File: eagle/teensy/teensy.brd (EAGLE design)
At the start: 51.7 x 35.5 mm, 4 parts

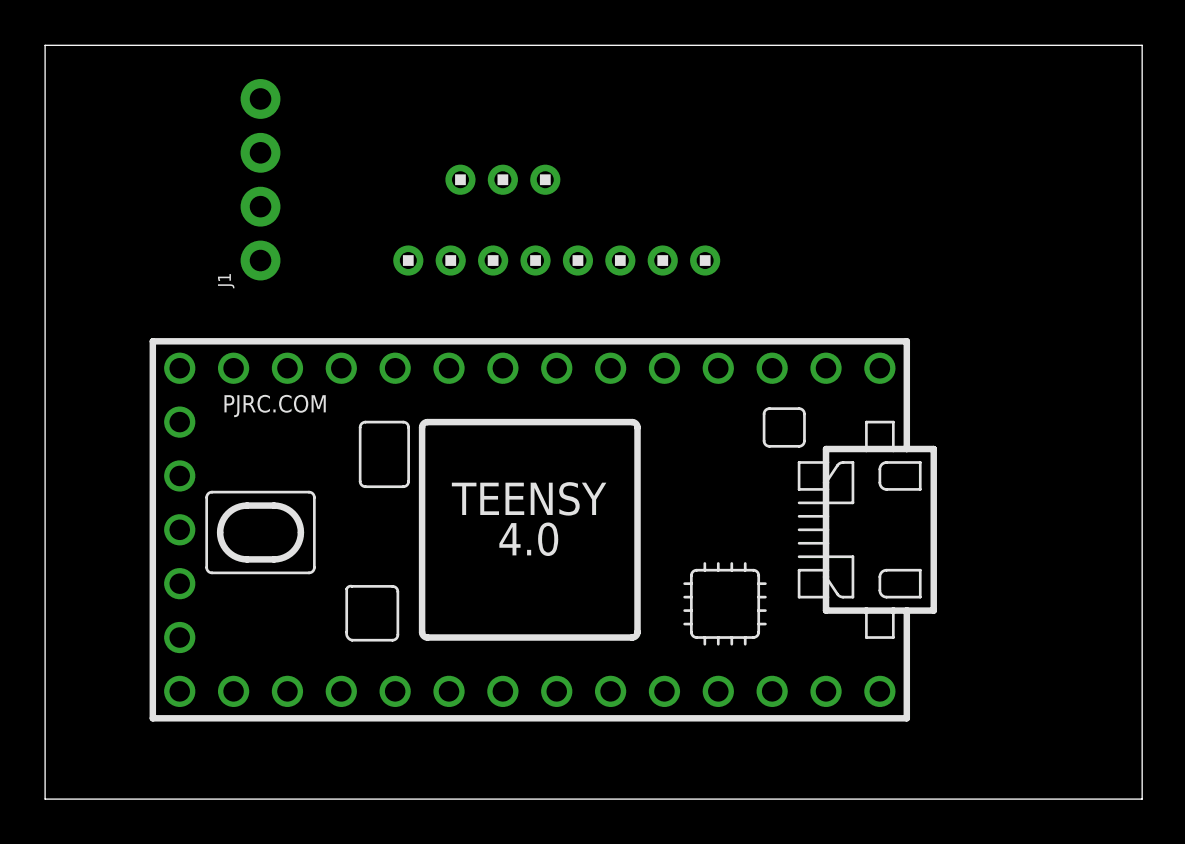
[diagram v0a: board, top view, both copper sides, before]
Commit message: modified:   eagle/teensy/teensy.brd
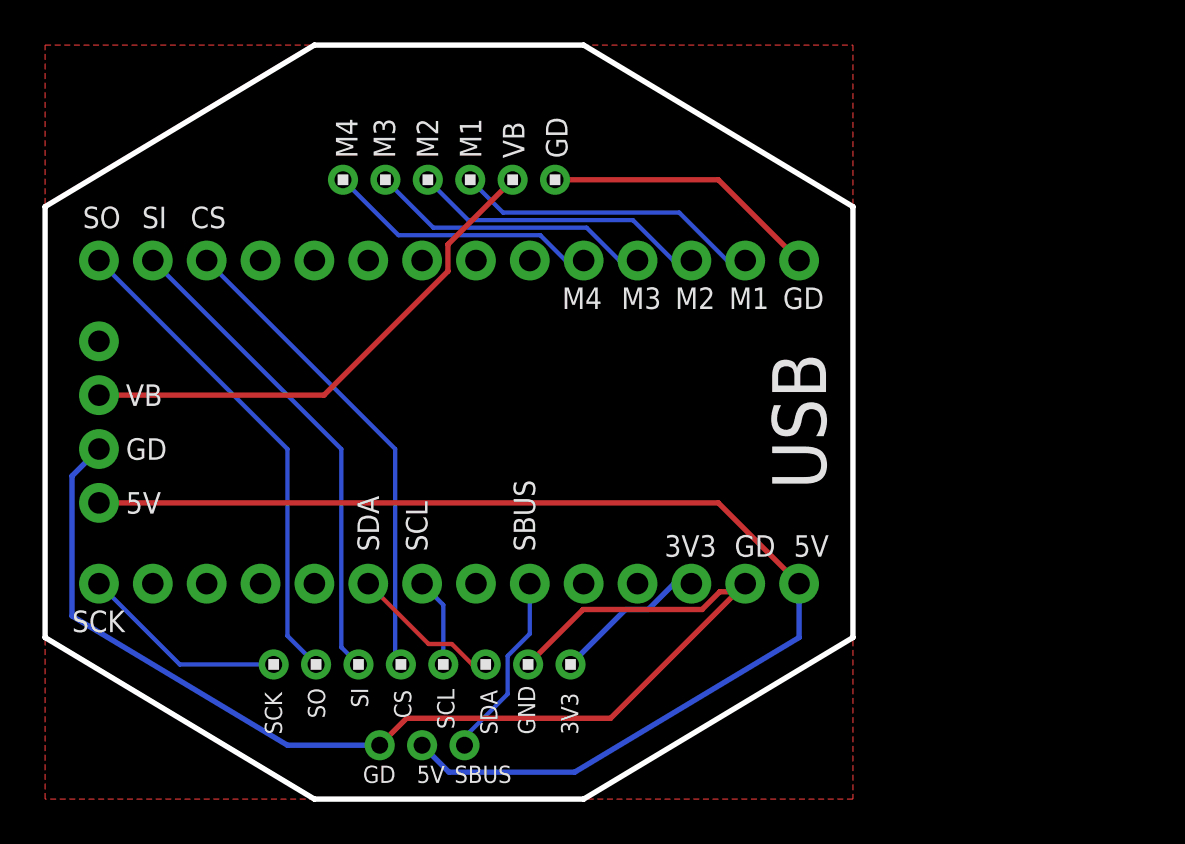
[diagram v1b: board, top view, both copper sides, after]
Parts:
- removed U$1: TEENSY_4.0, TEENSY 4.0:TEENSY_4.0
- added J2, J3: (no value), SparkFun-Connectors:1X14_NO_SILK
- added U$4: 1X6, headers(2mm):1X6
- moved U$2 26.9 mm to (17.8, 2.54), flipped to the bottom, turned to 180 degrees
- moved U$3 20.1 mm to (17.8, 6.35), turned to 180 degrees
- moved J1 8.52 mm to (2.54, 21.6), turned to 270 degrees
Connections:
- new net M1: J2.13, U$4.3
- new net M2: J2.12, U$4.4
- new net M3: J2.11, U$4.5
- new net M4: J2.10, U$4.6
- net 3V3: now also J3.12
- net 5V: now also J3.14
- net CS: now also J2.3, U$3.5; no longer U$3.8
- net GND: now also J2.14, J3.13, U$4.1
- net MISO: now also J2.1, U$3.7; no longer U$3.5
- net MOSI: now also J2.2
- net SBUS: now also J3.9
- net SCK: now also J3.1, U$3.8; no longer U$3.7
- net SCL: now also J3.7, U$3.4; no longer U$3.3
- net SDA: now also J3.6, U$3.3; no longer U$3.4
- net VBAT: now also U$4.2
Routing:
- net GND: track 0.00 -> 69.4 mm
- net 5V: track 0.00 -> 57.2 mm
- net VBAT: track 0.00 -> 24.5 mm
- net MISO: track 0.00 -> 23.3 mm
- net MOSI: track 0.00 -> 23.1 mm
- net CS: track 0.00 -> 22.8 mm
- net M1: track 0.00 -> 14.5 mm
- net M2: track 0.00 -> 14.0 mm
- net M3: track 0.00 -> 13.5 mm
- net M4: track 0.00 -> 12.9 mm
- net SCK: track 0.00 -> 9.82 mm
- net SBUS: track 0.00 -> 8.51 mm
- net 3V3: track 0.00 -> 7.28 mm
- net SDA: track 0.00 -> 7.12 mm
- net SCL: track 0.00 -> 4.22 mm
- added copper zone on layer 1, net GND
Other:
- board size 51.7 x 35.5 mm -> 38.1 x 35.6 mm
- board text added: "3V3"
- board text added: "5V"
- board text added: "CS"
- board text added: "GD"
- board text added: "GND"
- board text added: "M1"
- board text added: "M2"
- board text added: "M3"
- board text added: "M4"
- board text added: "SBUS"
- board text added: "SCK"
- board text added: "SCL"
- board text added: "SDA"
- board text added: "SI"
- board text added: "SO"
- board text added: "USB"
- board text added: "VB"

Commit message: modified:   eagle/teensy/teensy.brd
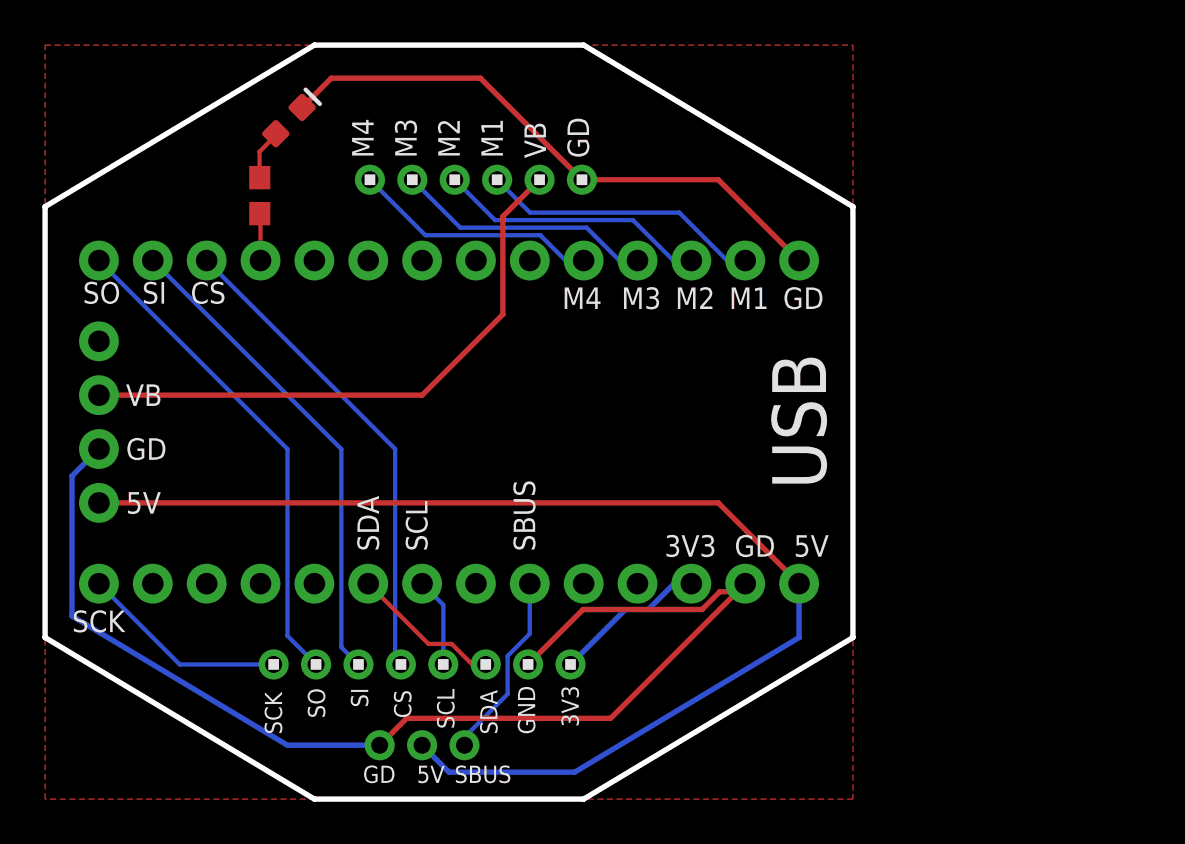
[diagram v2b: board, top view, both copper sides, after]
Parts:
- added D1: WHITE, SparkFun-LED:LED-0603
- added R1: 22, SparkFun-Resistors:0603
- moved U$4 1.27 mm to (20.3, 29.2)
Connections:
- new net R1: J2.4, R1.1
- new net R2: D1.A, R1.2
- net GND: now also D1.C
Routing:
- net GND: track 69.4 -> 83.8 mm
- net VBAT: track 24.5 -> 27.7 mm
- net R2: track 0.00 -> 2.39 mm
- net R1: track 0.00 -> 2.22 mm
- net M2: track 14.0 -> 12.7 mm
- net M4: track 12.9 -> 11.7 mm
- net M3: track 13.5 -> 12.2 mm
- net M1: track 14.5 -> 13.3 mm
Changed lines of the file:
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@@
 <setting verticaltext="up"/>
 </settings>
-<grid distance="10" unitdist="mil" unit="mil" style="lines" multiple="1" display="no" altdistance="5" altunitdist="mil" altunit="mil"/>
+<grid distance="0.000123031496" unitdist="mil" unit="mil" style="lines" multiple="1" display="no" altdistance="5" altunitdist="mil" altunit="mil"/>
 <layers>
 <layer number="1" name="Top" color="4" fill="1" visible="yes" active="yes"/>
@@
 <wire x1="12.7" y1="35.56" x2="25.4" y2="35.56" width="0.254" layer="20"/>
 <text x="36.83" y="14.605" size="2.54" layer="21" rot="R90">USB</text>
-<text x="14.732" y="30.226" size="1.016" layer="25" rot="R90">M4</text>
-<text x="16.51" y="30.226" size="1.016" layer="25" rot="R90">M3</text>
-<text x="18.542" y="30.226" size="1.016" layer="25" rot="R90">M2</text>
-<text x="20.574" y="30.226" size="1.016" layer="25" rot="R90">M1</text>
+<text x="15.494" y="30.226" size="1.016" layer="25" rot="R90">M4</text>
+<text x="17.526" y="30.226" size="1.016" layer="25" rot="R90">M3</text>
+<text x="19.558" y="30.226" size="1.016" layer="25" rot="R90">M2</text>
+<text x="21.59" y="30.226" size="1.016" layer="25" rot="R90">M1</text>
 <text x="3.81" y="18.542" size="1.016" layer="25">VB</text>
 <text x="3.81" y="16.002" size="1.016" layer="25">GD</text>
@@
 <text x="32.258" y="23.114" size="1.016" layer="25">M1</text>
 <text x="34.798" y="23.114" size="1.016" layer="25">GD</text>
-<text x="1.778" y="26.924" size="1.016" layer="25">SO</text>
-<text x="4.572" y="26.924" size="1.016" layer="25">SI</text>
-<text x="6.858" y="26.924" size="1.016" layer="25">CS</text>
-<text x="22.606" y="30.226" size="1.016" layer="25" rot="R90">VB</text>
-<text x="24.638" y="30.226" size="1.016" layer="25" rot="R90">GD</text>
+<text x="1.778" y="23.368" size="1.016" layer="25">SO</text>
+<text x="4.572" y="23.368" size="1.016" layer="25">SI</text>
+<text x="6.858" y="23.368" size="1.016" layer="25">CS</text>
+<text x="23.622" y="30.226" size="1.016" layer="25" rot="R90">VB</text>
+<text x="25.654" y="30.226" size="1.016" layer="25" rot="R90">GD</text>
 <text x="3.81" y="13.462" size="1.016" layer="25">5V</text>
 <text x="35.306" y="11.43" size="1.016" layer="25">5V</text>
@@
 <text x="21.336" y="3.048" size="0.8128" layer="25" rot="R90">SDA</text>
 <text x="23.114" y="3.048" size="0.8128" layer="25" rot="R90">GND</text>
-<text x="25.146" y="3.048" size="0.8128" layer="25" rot="R90">3V3</text>
+<text x="25.1709125" y="3.397071875" size="0.8128" layer="25" rot="R90">3V3</text>
 <text x="14.986" y="0.762" size="0.8128" layer="25">GD</text>
 <text x="17.526" y="0.762" size="0.8128" layer="25">5V</text>
@@
 <element name="U$2" library="headers(2mm)" package="1X3" value="1X3" x="17.78" y="2.54" smashed="yes" rot="MR180"/>
 <element name="U$3" library="headers(2mm)" package="1X8" value="1X8" x="17.78" y="6.35" smashed="yes" rot="R180"/>
-<element name="U$4" library="headers(2mm)" package="1X6" value="1X6" x="19.05" y="29.21" rot="R180"/>
+<element name="U$4" library="headers(2mm)" package="1X6" value="1X6" x="20.32" y="29.21" rot="R180"/>
 <element name="J2" library="SparkFun-Connectors" package="1X14_NO_SILK" value="" x="2.54" y="25.4" smashed="yes">
 <attribute name="VALUE" x="1.27" y="23.368" size="0.6096" layer="27" font="vector" ratio="20"/>
@@
 <element name="J3" library="SparkFun-Connectors" package="1X14_NO_SILK" value="" x="2.54" y="10.16" smashed="yes">
 <attribute name="VALUE" x="1.27" y="8.128" size="0.6096" layer="27" font="vector" ratio="20"/>
+</element>
+<element name="D1" library="SparkFun-LED" package="LED-0603" value="WHITE" x="11.5" y="32" smashed="yes" rot="R45">
+<attribute name="PROD_ID" value="DIO-09004" x="11.5" y="32" size="1.778" layer="27" rot="R45" display="off"/>
+</element>
+<element name="R1" library="SparkFun-Resistors" package="0603" value="22" x="10.12456875" y="28.458459375" smashed="yes" rot="R90">
+<attribute name="PROD_ID" value="RES-08698" x="10.12456875" y="28.458459375" size="1.778" layer="27" rot="R90" display="off"/>
 </element>
 </elements>
@@
 </polygon>
 <contactref element="J1" pad="3"/>
-<wire x1="24.05" y1="29.21" x2="31.75" y2="29.21" width="0.254" layer="1"/>
+<wire x1="25.32" y1="29.21" x2="31.75" y2="29.21" width="0.254" layer="1"/>
 <wire x1="31.75" y1="29.21" x2="35.56" y2="25.4" width="0.254" layer="1"/>
 <wire x1="26.67" y1="3.81" x2="17.05" y2="3.81" width="0.254" layer="1"/>
@@
 <wire x1="11.43" y1="2.54" x2="15.78" y2="2.54" width="0.254" layer="16"/>
 <wire x1="17.05" y1="3.81" x2="15.78" y2="2.54" width="0.254" layer="1"/>
+<contactref element="D1" pad="C"/>
+<wire x1="25.32" y1="29.21" x2="20.53" y2="34" width="0.254" layer="1"/>
+<wire x1="20.53" y1="34" x2="13.5" y2="34" width="0.254" layer="1"/>
+<wire x1="13.5" y1="34" x2="12.12013125" y2="32.62013125" width="0.254" layer="1"/>
 </signal>
 <signal name="5V">
@@
 <contactref element="J1" pad="2"/>
 <contactref element="U$4" pad="2"/>
-<wire x1="22.05" y1="29.21" x2="18.9992" y2="26.1592" width="0.254" layer="1"/>
-<wire x1="18.9992" y1="26.1592" x2="18.9992" y2="24.8949875" width="0.254" layer="1"/>
-<wire x1="18.9992" y1="24.8949875" x2="13.1542125" y2="19.05" width="0.254" layer="1"/>
-<wire x1="13.1542125" y1="19.05" x2="2.54" y2="19.05" width="0.254" layer="1"/>
+<wire x1="23.32" y1="29.21" x2="21.59" y2="27.48" width="0.254" layer="1"/>
+<wire x1="21.59" y1="27.48" x2="21.59" y2="22.86" width="0.254" layer="1"/>
+<wire x1="21.59" y1="22.86" x2="17.78" y2="19.05" width="0.254" layer="1"/>
+<wire x1="17.78" y1="19.05" x2="2.54" y2="19.05" width="0.254" layer="1"/>
 </signal>
 <signal name="SBUS">
@@
 <contactref element="U$4" pad="3"/>
 <contactref element="J2" pad="13"/>
-<wire x1="20.05" y1="29.21" x2="21.5994" y2="27.6606" width="0.2032" layer="16"/>
+<wire x1="21.32" y1="29.21" x2="22.8694" y2="27.6606" width="0.2032" layer="16"/>
 <wire x1="32.16829375" y1="25.4" x2="33.02" y2="25.4" width="0.2032" layer="16"/>
-<wire x1="21.5994" y1="27.6606" x2="29.90769375" y2="27.6606" width="0.2032" layer="16"/>
+<wire x1="22.8694" y1="27.6606" x2="29.90769375" y2="27.6606" width="0.2032" layer="16"/>
 <wire x1="29.90769375" y1="27.6606" x2="32.16829375" y2="25.4" width="0.2032" layer="16"/>
 </signal>
@@
 <contactref element="U$4" pad="4"/>
 <contactref element="J2" pad="12"/>
-<wire x1="18.05" y1="29.21" x2="19.955" y2="27.305" width="0.2032" layer="16"/>
+<wire x1="19.32" y1="29.21" x2="21.225" y2="27.305" width="0.2032" layer="16"/>
 <wire x1="29.62829375" y1="25.4" x2="30.48" y2="25.4" width="0.2032" layer="16"/>
-<wire x1="19.955" y1="27.305" x2="27.72329375" y2="27.305" width="0.2032" layer="16"/>
+<wire x1="21.225" y1="27.305" x2="27.72329375" y2="27.305" width="0.2032" layer="16"/>
 <wire x1="27.72329375" y1="27.305" x2="29.62829375" y2="25.4" width="0.2032" layer="16"/>
 </signal>
@@
 <contactref element="U$4" pad="5"/>
 <contactref element="J2" pad="11"/>
-<wire x1="16.05" y1="29.21" x2="18.3106" y2="26.9494" width="0.2032" layer="16"/>
+<wire x1="17.32" y1="29.21" x2="19.5806" y2="26.9494" width="0.2032" layer="16"/>
 <wire x1="27.08829375" y1="25.4" x2="27.94" y2="25.4" width="0.2032" layer="16"/>
-<wire x1="18.3106" y1="26.9494" x2="25.53889375" y2="26.9494" width="0.2032" layer="16"/>
+<wire x1="19.5806" y1="26.9494" x2="25.53889375" y2="26.9494" width="0.2032" layer="16"/>
 <wire x1="25.53889375" y1="26.9494" x2="27.08829375" y2="25.4" width="0.2032" layer="16"/>
 </signal>
@@
 <contactref element="U$4" pad="6"/>
 <contactref element="J2" pad="10"/>
-<wire x1="14.05" y1="29.21" x2="16.6662" y2="26.5938" width="0.2032" layer="16"/>
+<wire x1="15.32" y1="29.21" x2="17.9362" y2="26.5938" width="0.2032" layer="16"/>
 <wire x1="24.54829375" y1="25.4" x2="25.4" y2="25.4" width="0.2032" layer="16"/>
 <wire x1="23.35449375" y1="26.5938" x2="24.54829375" y2="25.4" width="0.2032" layer="16"/>
-<wire x1="16.6662" y1="26.5938" x2="23.35449375" y2="26.5938" width="0.2032" layer="16"/>
+<wire x1="17.9362" y1="26.5938" x2="23.35449375" y2="26.5938" width="0.2032" layer="16"/>
+</signal>
+<signal name="R2">
+<contactref element="D1" pad="A"/>
+<contactref element="R1" pad="2"/>
+<wire x1="10.879865625" y1="31.379865625" x2="10.879865625" y2="31.300015625" width="0.2032" layer="1"/>
+<wire x1="10.879865625" y1="31.300015625" x2="10.113484375" y2="30.533634375" width="0.2032" layer="1"/>
+<wire x1="10.113484375" y1="30.533634375" x2="10.113484375" y2="29.31954375" width="0.2032" layer="1"/>
+<wire x1="10.113484375" y1="29.31954375" x2="10.12456875" y2="29.308459375" width="0.2032" layer="1"/>
+</signal>
+<signal name="R1">
+<contactref element="R1" pad="1"/>
+<contactref element="J2" pad="4"/>
+<wire x1="10.16" y1="25.4" x2="10.16" y2="27.573028125" width="0.2032" layer="1"/>
+<wire x1="10.16" y1="27.573028125" x2="10.12456875" y2="27.608459375" width="0.2032" layer="1"/>
 </signal>
 </signals>
